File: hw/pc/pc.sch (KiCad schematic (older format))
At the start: 8 parts

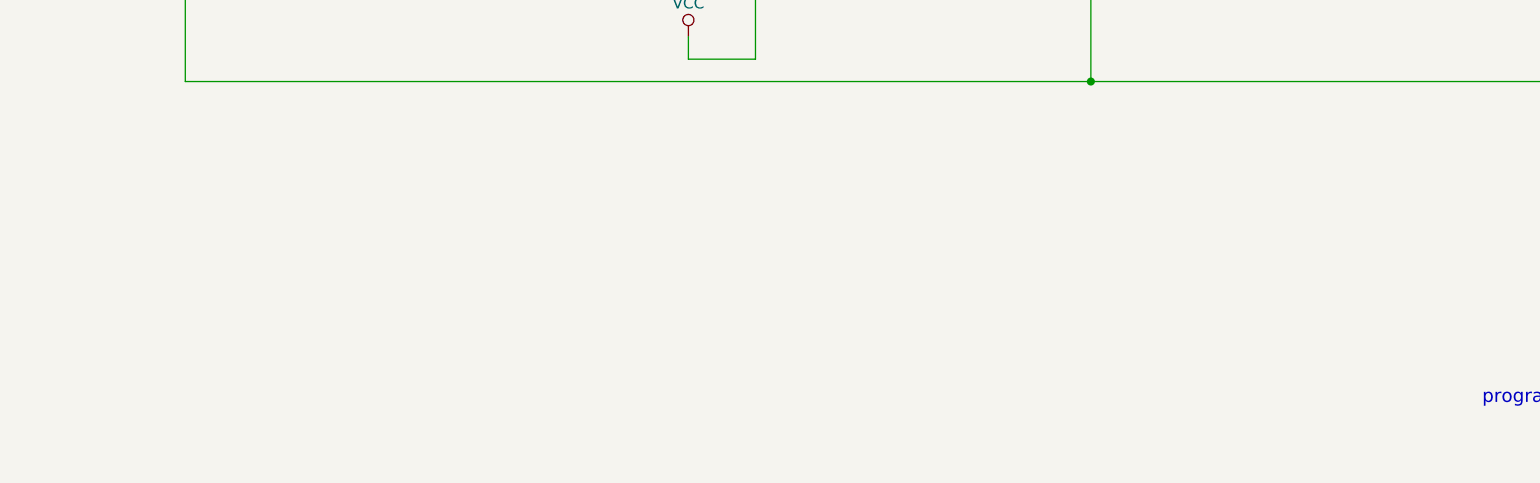
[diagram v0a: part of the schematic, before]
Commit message: added pair of '541 buffers for output to addr bus
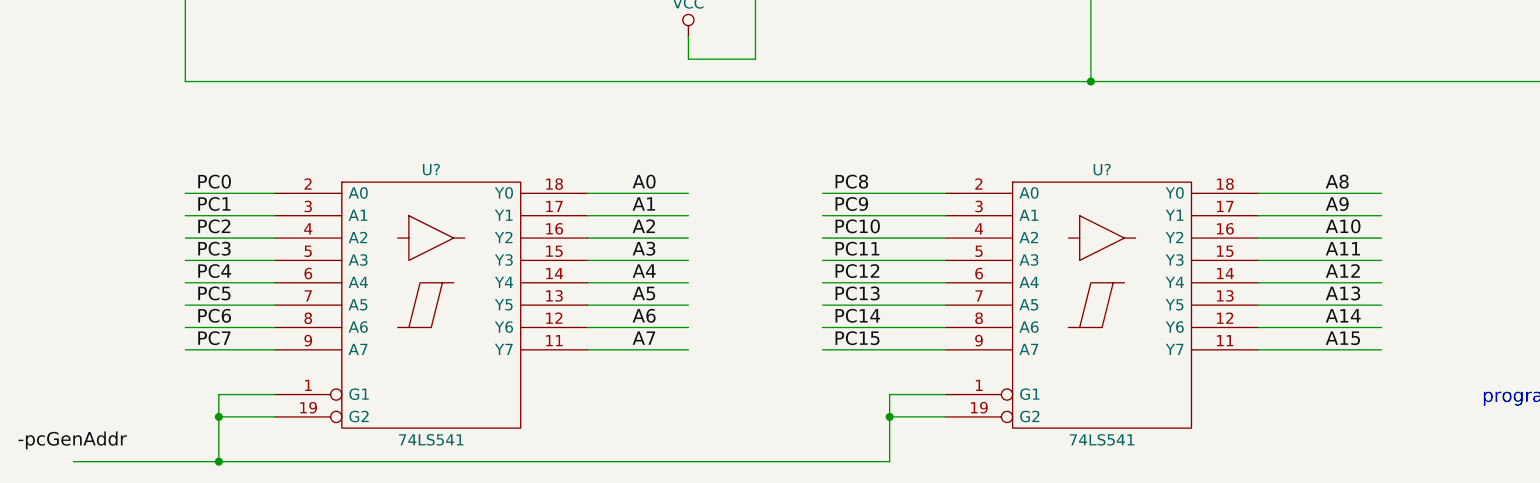
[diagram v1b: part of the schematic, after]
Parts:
- added U? (x2): 74LS541, symbol 74LS541
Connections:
- net labels added: -pcGenAddr, A0, A1, A10, A11, A12, A13, A14, A15, A2, A3, A4, A5, A6, A7, A8, A9
- wire segments 125 -> 164

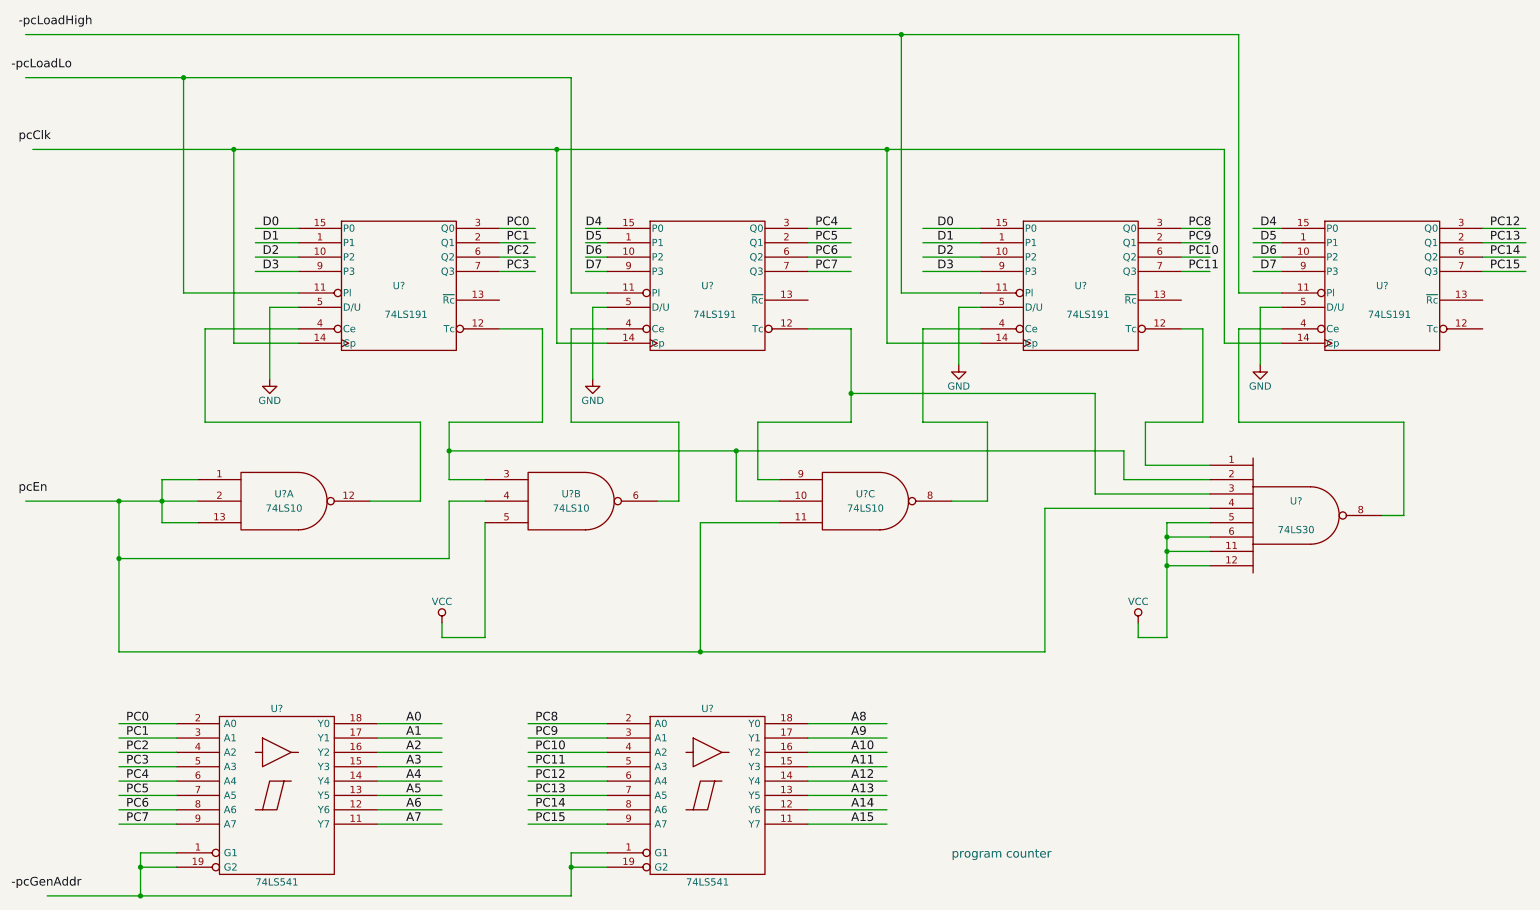
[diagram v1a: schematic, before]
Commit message: more accurate bus net labels
ALU data bus is ALU0..ALU7.

Left ALU input bus is LEFT0..LEFT7.

Right ALU input bus is RIGHT0..RIGHT7.
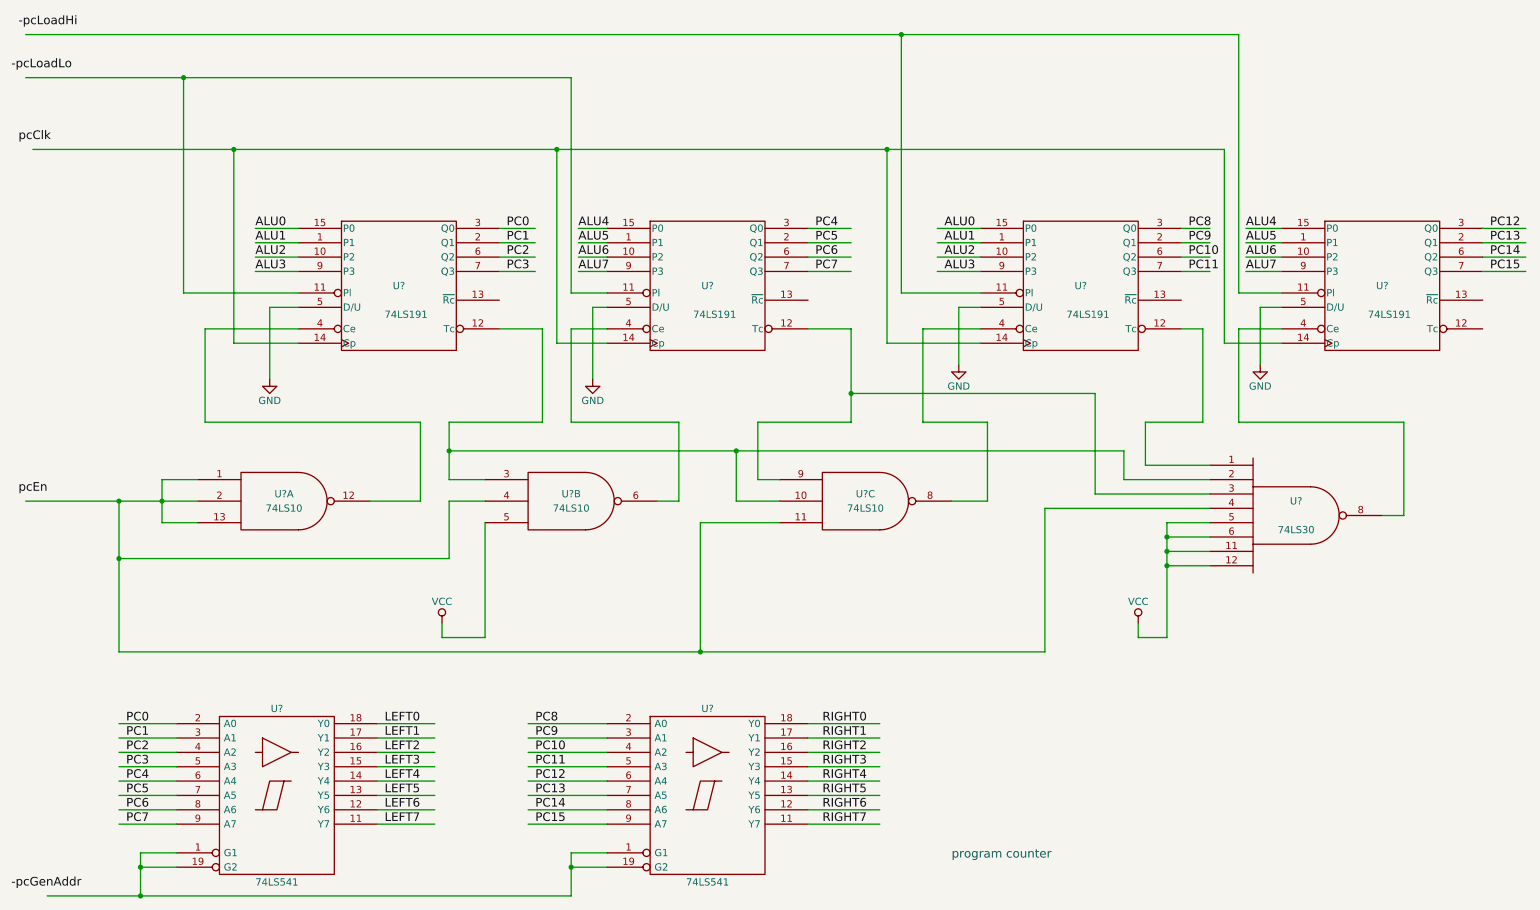
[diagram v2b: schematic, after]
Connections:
- net labels added: -pcLoadHi, ALU0, ALU1, ALU2, ALU3, ALU4, ALU5, ALU6, ALU7, LEFT0, LEFT1, LEFT2, LEFT3, LEFT4, LEFT5, LEFT6, LEFT7, RIGHT0, RIGHT1, RIGHT2, RIGHT3, RIGHT4, RIGHT5, RIGHT6, RIGHT7
- net labels removed: -pcLoadHigh, A0, A1, A10, A11, A12, A13, A14, A15, A2, A3, A4, A5, A6, A7, A8, A9, D0, D1, D2, D3, D4, D5, D6, D7
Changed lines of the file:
@@
 	1    0    0    -1
 $EndComp
-Text Label 2350 2350 0    60   ~ 0
-D0
-Text Label 2350 2450 0    60   ~ 0
-D1
-Text Label 2350 2550 0    60   ~ 0
-D2
-Text Label 2350 2650 0    60   ~ 0
-D3
-Text Label 7050 2350 0    60   ~ 0
-D0
-Text Label 7050 2450 0    60   ~ 0
-D1
-Text Label 7050 2550 0    60   ~ 0
-D2
-Text Label 7050 2650 0    60   ~ 0
-D3
 $Comp
 L 74LS10 U?
@@
 Text Notes 7150 6750 0    60   ~ 0
 program counter
-Text Label 4050 2350 0    60   ~ 0
-PC0
-Text Label 4050 2450 0    60   ~ 0
-PC1
-Text Label 4050 2550 0    60   ~ 0
-PC2
-Text Label 4050 2650 0    60   ~ 0
-PC3
-Text Label 6200 2350 0    60   ~ 0
-PC4
-Text Label 6200 2450 0    60   ~ 0
-PC5
-Text Label 6200 2550 0    60   ~ 0
-PC6
-Text Label 6200 2650 0    60   ~ 0
-PC7
-Text Label 8800 2350 0    60   ~ 0
-PC8
-Text Label 8800 2450 0    60   ~ 0
-PC9
-Text Label 8800 2550 0    60   ~ 0
-PC10
-Text Label 8800 2650 0    60   ~ 0
-PC11
 Text Label 10900 2350 0    60   ~ 0
 PC12
@@
 Text Label 650  1750 0    60   ~ 0
 pcClk
-Text Label 4600 2350 0    60   ~ 0
-D4
-Text Label 4600 2450 0    60   ~ 0
-D5
-Text Label 4600 2550 0    60   ~ 0
-D6
-Text Label 4600 2650 0    60   ~ 0
-D7
 Text Label 600  1250 0    60   ~ 0
 -pcLoadLo
-Text Label 9300 2350 0    60   ~ 0
-D4
-Text Label 9300 2450 0    60   ~ 0
-D5
-Text Label 9300 2550 0    60   ~ 0
-D6
-Text Label 9300 2650 0    60   ~ 0
-D7
 Text Label 650  950  0    60   ~ 0
--pcLoadHigh
+-pcLoadHi
 $Comp
 L 74LS541 U?
@@
 Text Label 1400 6500 0    60   ~ 0
 PC7
-Text Label 3350 5800 0    60   ~ 0
-A0
-Text Label 3350 5900 0    60   ~ 0
-A1
-Text Label 3350 6000 0    60   ~ 0
-A2
-Text Label 3350 6100 0    60   ~ 0
-A3
-Text Label 3350 6200 0    60   ~ 0
-A4
-Text Label 3350 6300 0    60   ~ 0
-A5
-Text Label 3350 6400 0    60   ~ 0
-A6
-Text Label 3350 6500 0    60   ~ 0
-A7
 Text Label 4250 5800 0    60   ~ 0
 PC8
@@
 Text Label 4250 6500 0    60   ~ 0
 PC15
-Text Label 6450 5800 0    60   ~ 0
-A8
-Text Label 6450 5900 0    60   ~ 0
-A9
-Text Label 6450 6000 0    60   ~ 0
-A10
-Text Label 6450 6100 0    60   ~ 0
-A11
-Text Label 6450 6200 0    60   ~ 0
-A12
-Text Label 6450 6300 0    60   ~ 0
-A13
-Text Label 6450 6400 0    60   ~ 0
-A14
-Text Label 6450 6500 0    60   ~ 0
-A15
-Wire Wire Line
-	2600 2350 2300 2350
-Wire Wire Line
-	2600 2450 2300 2450
-Wire Wire Line
-	2600 2550 2300 2550
-Wire Wire Line
-	2600 2650 2300 2650
-Wire Wire Line
-	7350 2350 6950 2350
-Wire Wire Line
-	7350 2450 6950 2450
-Wire Wire Line
-	7350 2550 6950 2550
-Wire Wire Line
-	7350 2650 6950 2650
 Wire Wire Line
 	700  4250 1900 4250
@@
 Connection ~ 8650 4700
 Wire Wire Line
-	4000 2350 4250 2350
-Wire Wire Line
-	4000 2450 4250 2450
-Wire Wire Line
-	4000 2550 4250 2550
-Wire Wire Line
-	4000 2650 4250 2650
-Wire Wire Line
-	6150 2350 6450 2350
-Wire Wire Line
-	6150 2450 6450 2450
-Wire Wire Line
-	6150 2550 6450 2550
-Wire Wire Line
-	6150 2650 6450 2650
-Wire Wire Line
-	8750 2350 8950 2350
-Wire Wire Line
-	8750 2450 8950 2450
-Wire Wire Line
-	8750 2550 8950 2550
-Wire Wire Line
-	8750 2650 8950 2650
-Wire Wire Line
 	10850 2350 11150 2350
 Wire Wire Line
@@
 Connection ~ 6700 1800
 Wire Wire Line
-	4750 2350 4600 2350
-Wire Wire Line
-	4750 2450 4600 2450
-Wire Wire Line
-	4750 2550 4600 2550
-Wire Wire Line
-	4750 2650 4600 2650
-Wire Wire Line
 	4750 3150 4400 3150
 Wire Wire Line
@@
 	700  1000 9150 1000
 Wire Wire Line
-	9450 2350 9250 2350
-Wire Wire Line
-	9450 2450 9250 2450
-Wire Wire Line
-	9450 2550 9250 2550
-Wire Wire Line
-	9450 2650 9250 2650
-Wire Wire Line
 	9450 2800 9150 2800
 Wire Wire Line
@@
 	1750 6500 1350 6500
 Wire Wire Line
-	3150 5800 3600 5800
-Wire Wire Line
-	3150 5900 3600 5900
-Wire Wire Line
-	3150 6000 3600 6000
-Wire Wire Line
-	3150 6100 3600 6100
-Wire Wire Line
-	3150 6200 3600 6200
-Wire Wire Line
-	3150 6300 3600 6300
-Wire Wire Line
-	3150 6400 3600 6400
-Wire Wire Line
-	3150 6500 3600 6500
-Wire Wire Line
 	4750 5800 4200 5800
 Wire Wire Line
@@
 Wire Wire Line
 	4750 6500 4200 6500
-Wire Wire Line
-	6150 5800 6700 5800
-Wire Wire Line
-	6150 5900 6700 5900
-Wire Wire Line
-	6150 6000 6700 6000
-Wire Wire Line
-	6150 6100 6700 6100
-Wire Wire Line
-	6150 6200 6700 6200
-Wire Wire Line
-	6150 6300 6700 6300
-Wire Wire Line
-	6150 6400 6700 6400
-Wire Wire Line
-	6150 6500 6700 6500
 Wire Wire Line
 	1750 6700 1500 6700
@@
 Text Label 600  6950 0    60   ~ 0
 -pcGenAddr
+Wire Wire Line
+	8750 2650 8950 2650
+Wire Wire Line
+	8750 2550 8950 2550
+Wire Wire Line
+	8750 2450 8950 2450
+Wire Wire Line
+	8750 2350 8950 2350
+Text Label 8800 2650 0    60   ~ 0
+PC11
+Text Label 8800 2550 0    60   ~ 0
+PC10
+Text Label 8800 2450 0    60   ~ 0
+PC9
+Text Label 8800 2350 0    60   ~ 0
+PC8
+Text Label 6200 2650 0    60   ~ 0
+PC7
+Text Label 6200 2550 0    60   ~ 0
+PC6
+Text Label 6200 2450 0    60   ~ 0
+PC5
+Text Label 6200 2350 0    60   ~ 0
+PC4
+Wire Wire Line
+	6150 2650 6450 2650
+Wire Wire Line
+	6150 2550 6450 2550
+Wire Wire Line
+	6150 2450 6450 2450
+Wire Wire Line
+	6150 2350 6450 2350
+Wire Wire Line
+	4000 2650 4250 2650
+Wire Wire Line
+	4000 2550 4250 2550
+Wire Wire Line
+	4000 2450 4250 2450
+Wire Wire Line
+	4000 2350 4250 2350
+Text Label 4050 2650 0    60   ~ 0
+PC3
+Text Label 4050 2550 0    60   ~ 0
+PC2
+Text Label 4050 2450 0    60   ~ 0
+PC1
+Text Label 4050 2350 0    60   ~ 0
+PC0
+Wire Wire Line
+	2600 2350 2300 2350
+Wire Wire Line
+	2600 2450 2300 2450
+Wire Wire Line
+	2600 2550 2300 2550
+Wire Wire Line
+	2600 2650 2300 2650
+Text Label 2300 2350 0    60   ~ 0
+ALU0
+Text Label 2300 2450 0    60   ~ 0
+ALU1
+Text Label 2300 2550 0    60   ~ 0
+ALU2
+Text Label 2300 2650 0    60   ~ 0
+ALU3
+Wire Wire Line
+	4750 2350 4550 2350
+Wire Wire Line
+	4750 2450 4550 2450
+Wire Wire Line
+	4750 2550 4550 2550
+Wire Wire Line
+	4750 2650 4550 2650
+Text Label 4550 2350 0    60   ~ 0
+ALU4
+Text Label 4550 2450 0    60   ~ 0
+ALU5
+Text Label 4550 2550 0    60   ~ 0
+ALU6
+Text Label 4550 2650 0    60   ~ 0
+ALU7
+Wire Wire Line
+	7350 2350 7050 2350
+Wire Wire Line
+	7350 2450 7050 2450
+Wire Wire Line
+	7350 2550 7050 2550
+Wire Wire Line
+	7350 2650 7050 2650
+Text Label 7100 2350 0    60   ~ 0
+ALU0
+Text Label 7100 2450 0    60   ~ 0
+ALU1
+Text Label 7100 2550 0    60   ~ 0
+ALU2
+Text Label 7100 2650 0    60   ~ 0
+ALU3
+Wire Wire Line
+	9450 2350 9200 2350
+Wire Wire Line
+	9450 2450 9200 2450
+Wire Wire Line
+	9450 2550 9200 2550
+Wire Wire Line
+	9450 2650 9200 2650
+Text Label 9200 2350 0    60   ~ 0
+ALU4
+Text Label 9200 2450 0    60   ~ 0
+ALU5
+Text Label 9200 2550 0    60   ~ 0
+ALU6
+Text Label 9200 2650 0    60   ~ 0
+ALU7
+Wire Wire Line
+	3150 5800 3550 5800
+Wire Wire Line
+	3150 5900 3550 5900
+Wire Wire Line
+	3150 6000 3550 6000
+Wire Wire Line
+	3150 6100 3550 6100
+Wire Wire Line
+	3150 6200 3550 6200
+Wire Wire Line
+	3150 6300 3550 6300
+Wire Wire Line
+	3150 6400 3550 6400
+Wire Wire Line
+	3150 6500 3550 6500
+Text Label 3200 5800 0    60   ~ 0
+LEFT0
+Text Label 3200 5900 0    60   ~ 0
+LEFT1
+Text Label 3200 6000 0    60   ~ 0
+LEFT2
+Text Label 3200 6100 0    60   ~ 0
+LEFT3
+Text Label 3200 6200 0    60   ~ 0
+LEFT4
+Text Label 3200 6300 0    60   ~ 0
+LEFT5
+Text Label 3200 6400 0    60   ~ 0
+LEFT6
+Text Label 3200 6500 0    60   ~ 0
+LEFT7
+Wire Wire Line
+	6150 5800 6650 5800
+Wire Wire Line
+	6150 5900 6650 5900
+Wire Wire Line
+	6150 6000 6650 6000
+Wire Wire Line
+	6150 6100 6650 6100
+Wire Wire Line
+	6150 6200 6650 6200
+Wire Wire Line
+	6150 6300 6650 6300
+Wire Wire Line
+	6150 6400 6650 6400
+Wire Wire Line
+	6150 6500 6650 6500
+Text Label 6250 5800 0    60   ~ 0
+RIGHT0
+Text Label 6250 5900 0    60   ~ 0
+RIGHT1
+Text Label 6250 6000 0    60   ~ 0
+RIGHT2
+Text Label 6250 6100 0    60   ~ 0
+RIGHT3
+Text Label 6250 6200 0    60   ~ 0
+RIGHT4
+Text Label 6250 6300 0    60   ~ 0
+RIGHT5
+Text Label 6250 6400 0    60   ~ 0
+RIGHT6
+Text Label 6250 6500 0    60   ~ 0
+RIGHT7
 $EndSCHEMATC
